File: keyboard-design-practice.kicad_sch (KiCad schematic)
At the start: 21 parts

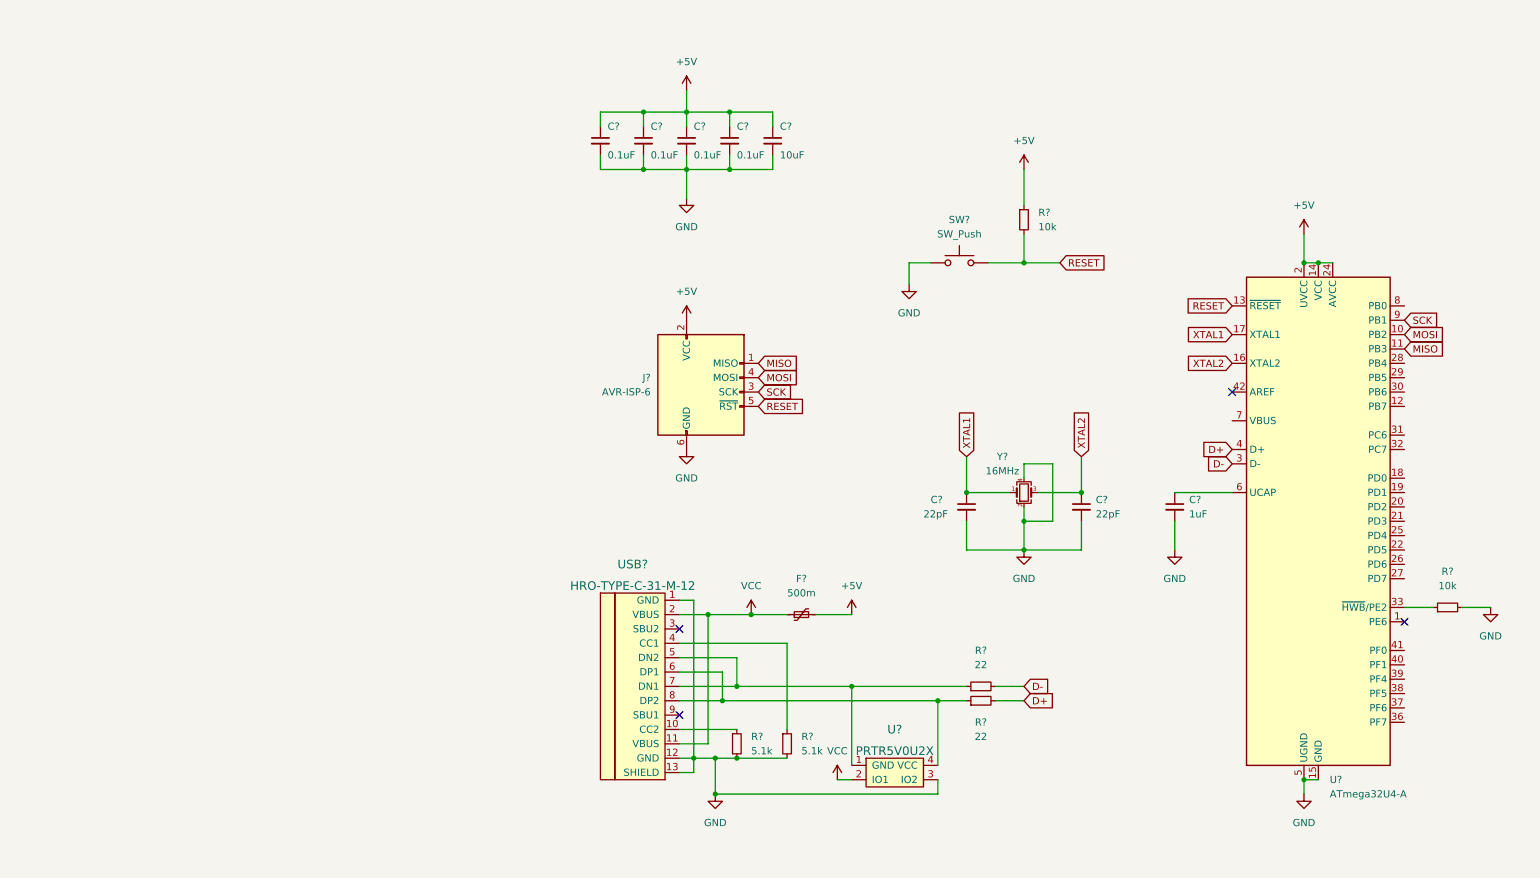
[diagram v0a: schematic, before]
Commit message: Created the key matrix
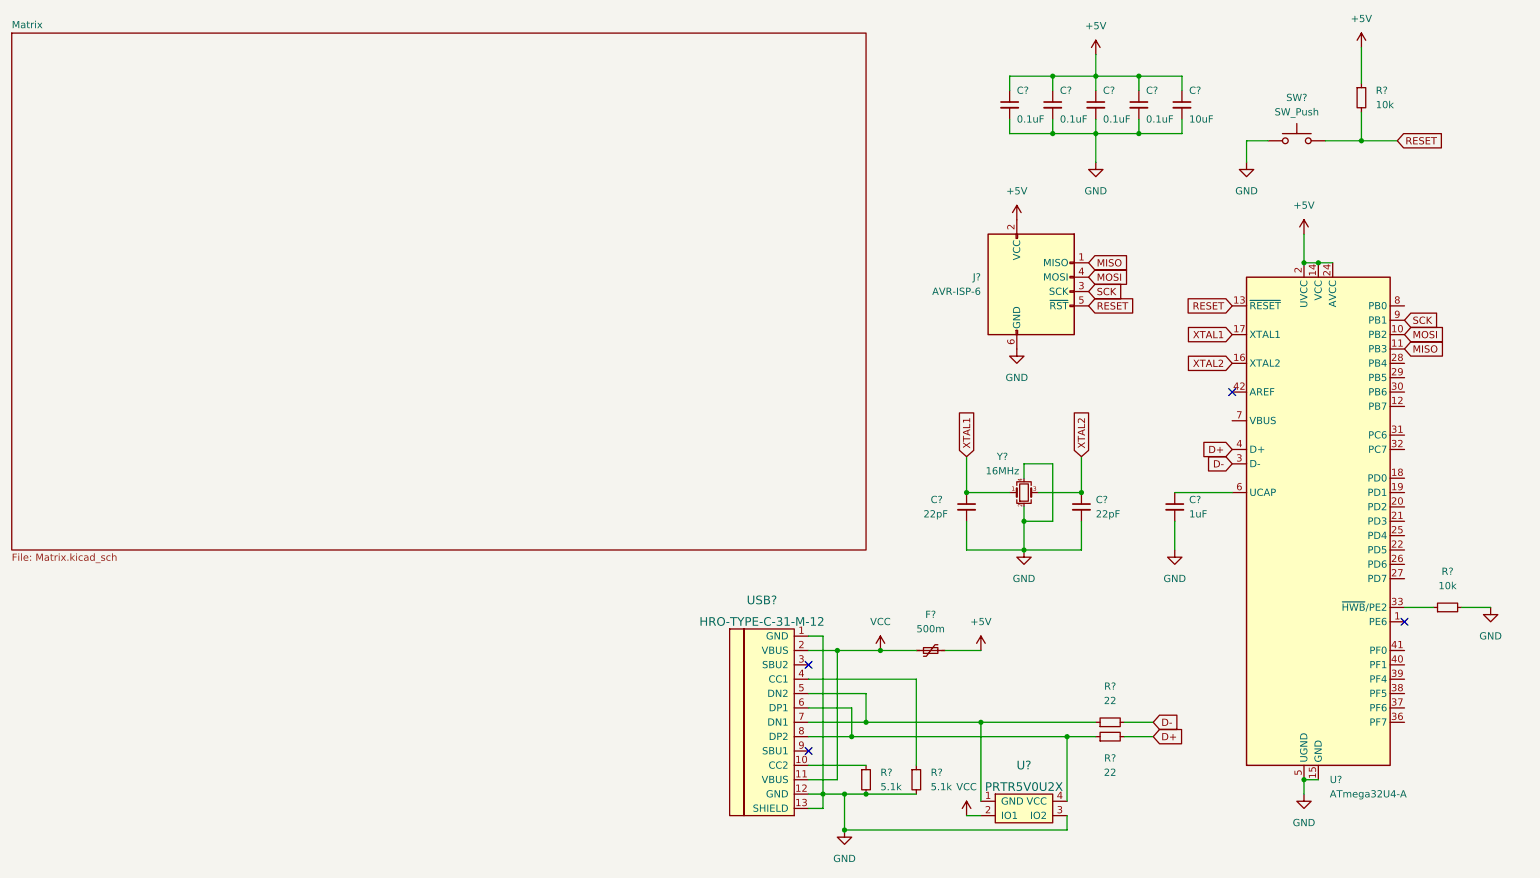
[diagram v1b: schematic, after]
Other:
- added sheet Matrix (Matrix.kicad_sch)
- moved on the sheet: C?, F?, J?, R?, SW?, U?, USB?

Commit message: Assigned the columns and rows to the MCU
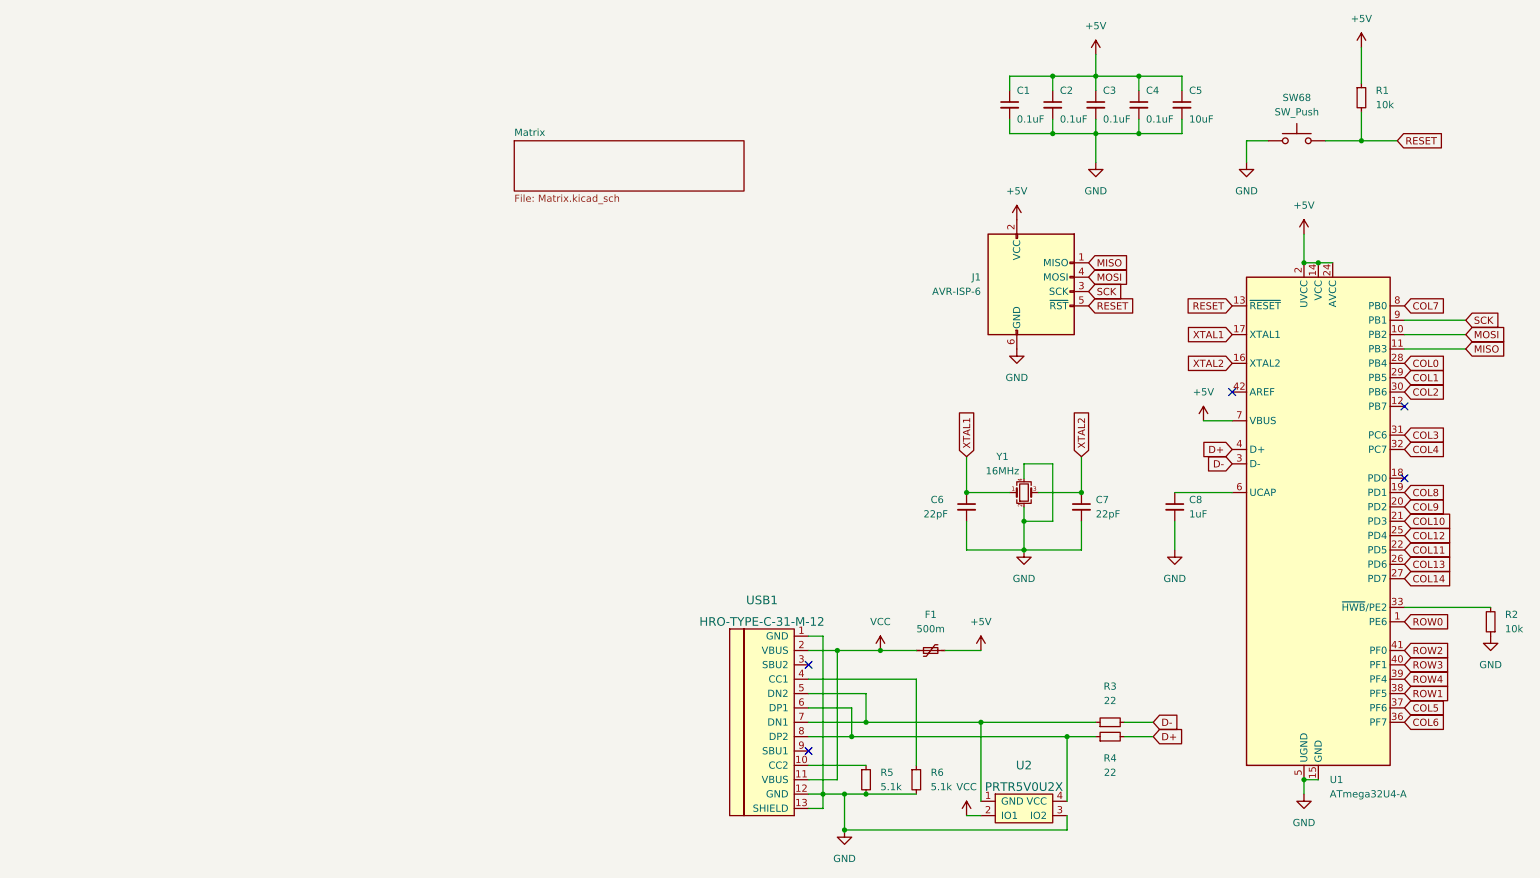
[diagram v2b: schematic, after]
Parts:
- gave numbers to parts that had none: 21
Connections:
- net +5V: now also U1.7 (VBUS)
- net GND: now also R2.1; no longer R2.2
- net at U1.33 (~{HWB}/PE2): now also R2.2; no longer R2.1
- net ROW0: now reaches U1.1 (PE6)
- net COL8: now reaches U1.19 (PD1)
- net COL9: now reaches U1.20 (PD2)
- net COL10: now reaches U1.21 (PD3)
- net COL11: now reaches U1.22 (PD5)
- net COL12: now reaches U1.25 (PD4)
- net COL13: now reaches U1.26 (PD6)
- net COL14: now reaches U1.27 (PD7)
- net COL0: now reaches U1.28 (PB4)
- net COL1: now reaches U1.29 (PB5)
- net COL2: now reaches U1.30 (PB6)
- net COL3: now reaches U1.31 (PC6)
- net COL4: now reaches U1.32 (PC7)
- net COL6: now reaches U1.36 (PF7)
- net COL5: now reaches U1.37 (PF6)
- net ROW1: now reaches U1.38 (PF5)
- net ROW4: now reaches U1.39 (PF4)
- net ROW3: now reaches U1.40 (PF1)
- net ROW2: now reaches U1.41 (PF0)
- net COL7: now reaches U1.8 (PB0)
- no-connect marks 4 -> 5
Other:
- moved on the sheet: R2

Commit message: ERC done
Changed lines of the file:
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@@
 (kicad_sch (version 20211123) (generator eeschema)
   (paper "A4")
+  (junction (at 168.91 128.27) (diameter 0) (color 0 0 0 0)
+  )
   (junction (at 218.44 26.67) (diameter 0) (color 0 0 0 0)
   )
@@
   (junction (at 247.65 151.13) (diameter 0) (color 0 0 0 0)
   )
+  (junction (at 186.69 128.27) (diameter 0) (color 0 0 0 0)
+  )
   (junction (at 170.18 153.67) (diameter 0) (color 0 0 0 0)
   )
@@
   )
   (junction (at 198.12 110.49) (diameter 0) (color 0 0 0 0)
+  )
+  (junction (at 161.29 156.21) (diameter 0) (color 0 0 0 0)
   )
   (junction (at 205.74 143.51) (diameter 0) (color 0 0 0 0)
@@
     (stroke (width 0) (type default) (color 0 0 0 0))
   )
+  (wire (pts (xy 186.69 128.27) (xy 190.5 128.27))
+    (stroke (width 0) (type default) (color 0 0 0 0))
+  )
   (wire (pts (xy 160.02 153.67) (xy 162.56 153.67))
     (stroke (width 0) (type default) (color 0 0 0 0))
@@
     (stroke (width 0) (type default) (color 0 0 0 0))
   )
-  (wire (pts (xy 160.02 156.21) (xy 162.56 156.21))
-    (stroke (width 0) (type default) (color 0 0 0 0))
-  )
-  (wire (pts (xy 184.15 128.27) (xy 190.5 128.27))
+  (wire (pts (xy 160.02 156.21) (xy 161.29 156.21))
+    (stroke (width 0) (type default) (color 0 0 0 0))
+  )
+  (wire (pts (xy 184.15 128.27) (xy 186.69 128.27))
     (stroke (width 0) (type default) (color 0 0 0 0))
   )
@@
     (stroke (width 0) (type default) (color 0 0 0 0))
   )
+  (wire (pts (xy 161.29 156.21) (xy 162.56 156.21))
+    (stroke (width 0) (type default) (color 0 0 0 0))
+  )
   (wire (pts (xy 208.28 110.49) (xy 198.12 110.49))
     (stroke (width 0) (type default) (color 0 0 0 0))
@@
     (stroke (width 0) (type default) (color 0 0 0 0))
   )
-  (wire (pts (xy 165.1 128.27) (xy 172.72 128.27))
+  (wire (pts (xy 165.1 128.27) (xy 168.91 128.27))
     (stroke (width 0) (type default) (color 0 0 0 0))
   )
@@
   )
   (wire (pts (xy 162.56 125.73) (xy 160.02 125.73))
+    (stroke (width 0) (type default) (color 0 0 0 0))
+  )
+  (wire (pts (xy 168.91 128.27) (xy 172.72 128.27))
     (stroke (width 0) (type default) (color 0 0 0 0))
   )
@@
     (pin "1")
   )
+  (symbol (lib_id "power:PWR_FLAG") (at 168.91 128.27 0) (unit 1)
+    (in_bom yes) (on_board yes) (fields_autoplaced)
+    (property "Reference" "#FLG0103" (id 0) (at 168.91 126.365 0)
+      (effects (font (size 1.27 1.27)) hide)
+    )
+    (property "Value" "PWR_FLAG" (id 1) (at 168.91 123.19 0))
+    (property "Footprint" "" (id 2) (at 168.91 128.27 0)
+      (effects (font (size 1.27 1.27)) hide)
+    )
+    (property "Datasheet" "~" (id 3) (at 168.91 128.27 0)
+      (effects (font (size 1.27 1.27)) hide)
+    )
+    (pin "1")
+  )
   (symbol (lib_id "power:GND") (at 224.79 110.49 0) (unit 1)
     (in_bom yes) (on_board yes) (fields_autoplaced)
@@
   (symbol (lib_id "power:+5V") (at 229.87 87.63 0) (unit 1)
     (in_bom yes) (on_board yes) (fields_autoplaced)
-    (property "Reference" "#PWR?" (id 0) (at 229.87 91.44 0)
+    (property "Reference" "#PWR0101" (id 0) (at 229.87 91.44 0)
       (effects (font (size 1.27 1.27)) hide)
     )
@@
     (pin "2")
   )
+  (symbol (lib_id "power:PWR_FLAG") (at 186.69 128.27 0) (unit 1)
+    (in_bom yes) (on_board yes) (fields_autoplaced)
+    (property "Reference" "#FLG0102" (id 0) (at 186.69 126.365 0)
+      (effects (font (size 1.27 1.27)) hide)
+    )
+    (property "Value" "PWR_FLAG" (id 1) (at 186.69 123.19 0))
+    (property "Footprint" "" (id 2) (at 186.69 128.27 0)
+      (effects (font (size 1.27 1.27)) hide)
+    )
+    (property "Datasheet" "~" (id 3) (at 186.69 128.27 0)
+      (effects (font (size 1.27 1.27)) hide)
+    )
+    (pin "1")
+  )
   (symbol (lib_id "Device:R_Small") (at 179.07 151.13 0) (unit 1)
     (in_bom yes) (on_board yes) (fields_autoplaced)
@@
     (pin "1")
     (pin "2")
+  )
+  (symbol (lib_id "power:PWR_FLAG") (at 161.29 156.21 180) (unit 1)
+    (in_bom yes) (on_board yes) (fields_autoplaced)
+    (property "Reference" "#FLG0101" (id 0) (at 161.29 158.115 0)
+      (effects (font (size 1.27 1.27)) hide)
+    )
+    (property "Value" "PWR_FLAG" (id 1) (at 161.29 161.29 0))
+    (property "Footprint" "" (id 2) (at 161.29 156.21 0)
+      (effects (font (size 1.27 1.27)) hide)
+    )
+    (property "Datasheet" "~" (id 3) (at 161.29 156.21 0)
+      (effects (font (size 1.27 1.27)) hide)
+    )
+    (pin "1")
   )
   (symbol (lib_id "Device:C_Small") (at 208.28 102.87 0) (unit 1)
@@
   )
   (symbol_instances
+    (path "/fa12e3ae-bd8b-4466-9d38-c23a59e8d7e8"
+      (reference "#FLG0101") (unit 1) (value "PWR_FLAG") (footprint "")
+    )
+    (path "/f715fa42-b3be-4b47-b370-efe542afb8f1"
+      (reference "#FLG0102") (unit 1) (value "PWR_FLAG") (footprint "")
+    )
+    (path "/9d81fd56-a084-489d-959c-2d5028c9ed94"
+      (reference "#FLG0103") (unit 1) (value "PWR_FLAG") (footprint "")
+    )
     (path "/e1534bad-e8c4-49dc-92a6-ef34c3fa8757"
       (reference "#PWR01") (unit 1) (value "+5V") (footprint "")
@@
     )
     (path "/d960e0b7-b92f-47d4-9235-f3bf95b3c3cf"
-      (reference "#PWR?") (unit 1) (value "+5V") (footprint "")
+      (reference "#PWR0101") (unit 1) (value "+5V") (footprint "")
     )
     (path "/f13a73ed-c874-4644-ae87-4ff3f132daae"

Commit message: Schema finished
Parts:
- C1, C2, C3, C4, C5, C6, C7, C8: footprint (none) -> Capacitor_SMD:C_0805_2012Metric_Pad1.18x1.45mm_HandSolder
- F1: footprint (none) -> Fuse:Fuse_1206_3216Metric_Pad1.42x1.75mm_HandSolder
- J1: footprint (none) -> random-keyboard-parts:Reset_Pretty-Mask
- R1, R2, R3, R4, R5, R6: footprint (none) -> Resistor_SMD:R_0805_2012Metric_Pad1.20x1.40mm_HandSolder
- SW68: footprint (none) -> Button_Switch_SMD:SW_SPST_SKQG_WithStem
- U2: footprint (none) -> random-keyboard-parts:SOT143B
- USB1: footprint (none) -> Type-C:HRO-TYPE-C-31-M-12-HandSoldering
- Y1: footprint (none) -> Crystal:Crystal_SMD_3225-4Pin_3.2x2.5mm_HandSoldering
